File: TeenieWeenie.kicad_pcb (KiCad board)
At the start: 4 copper layers, 50.8 x 101.6 mm, 118 parts, among them J1 Barrel_Jack, J2 Conn_01x01, J3 Conn_01x01, J4 Conn_01x01, J5 Conn_01x01, J6 Conn_01x01, J8 Conn_01x01, Q1 DMP2160UW-7, SW1 SW_Push, U1 WM8904CGEFL/V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

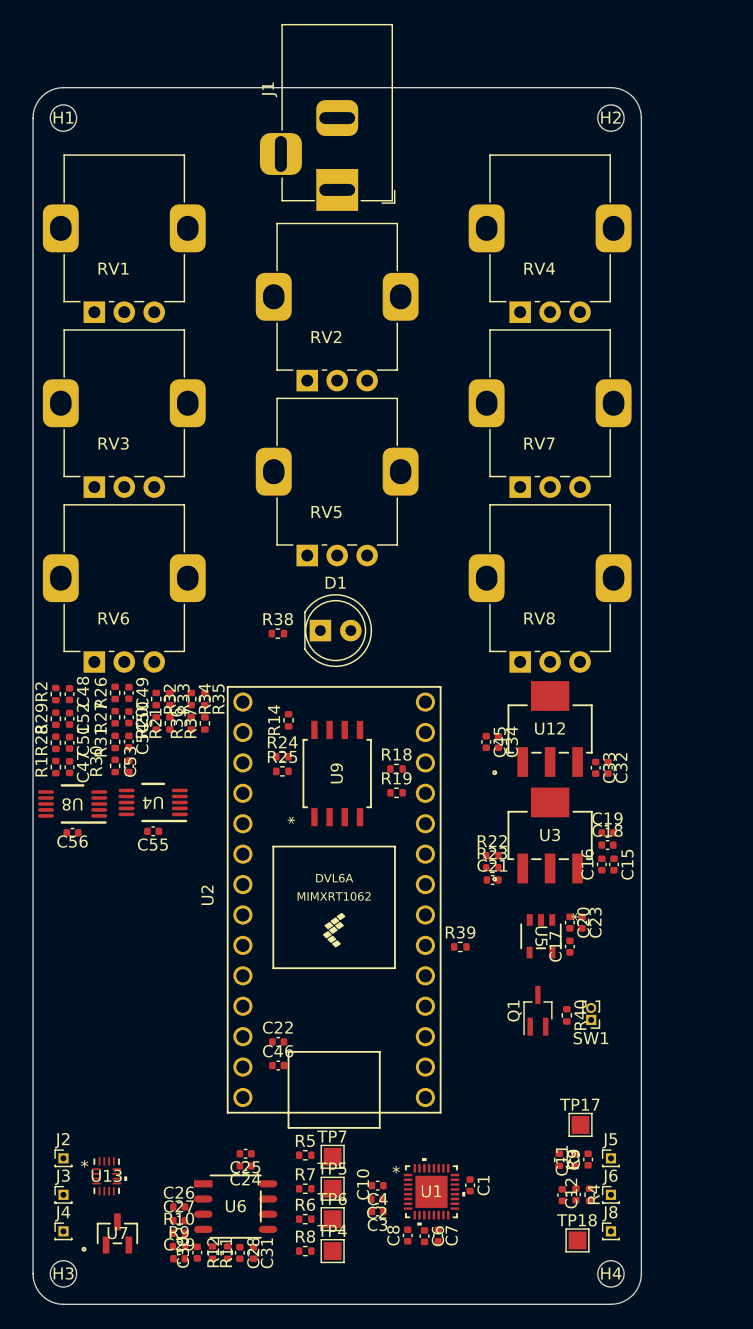
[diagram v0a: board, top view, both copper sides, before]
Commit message: routed power
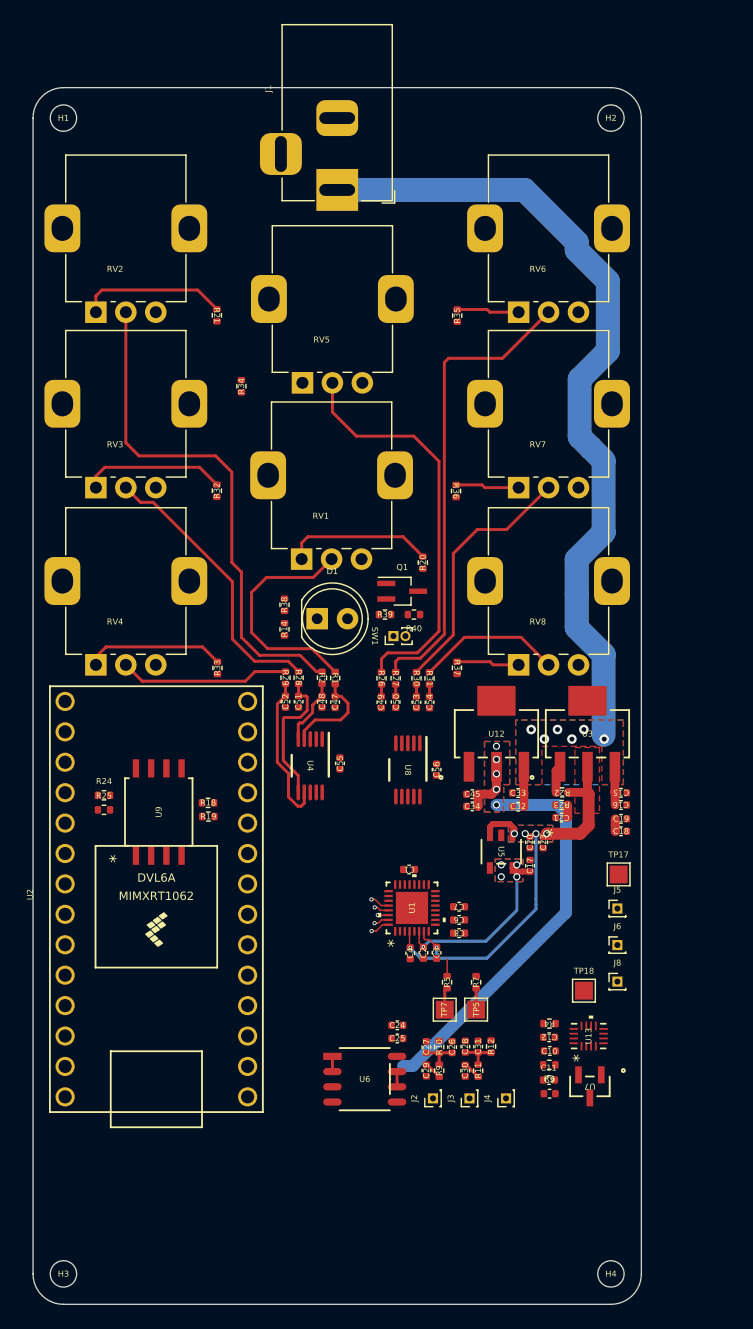
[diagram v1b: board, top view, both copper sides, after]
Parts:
- removed C22: 10u, Capacitor_SMD:C_0402_1005Metric
- removed C46: 0.1u, Capacitor_SMD:C_0402_1005Metric
- removed R6, R8: 0, Resistor_SMD:R_0402_1005Metric
- removed TP4, TP6: TestPoint, TestPoint:TestPoint_Pad_1.5x1.5mm
- moved RV4 46.1 mm to (99.2, 73.6)
- moved RV6 45.9 mm to (134.5, 44.1)
- moved U13 41.9 mm to (140.4, 104.6), turned to 90 degrees
- moved U7 41.3 mm to (140.5, 108.8), turned to 180 degrees
- moved J4 38.6 mm to (133.5, 109.8), turned to 90 degrees
- moved R35 38.3 mm to (129.4, 44.4)
- moved Q1 36.8 mm to (124.8, 67.5), turned to 0 degrees
- moved SW1 36.1 mm to (124.1, 71.2), turned to 90 degrees
- moved R40 35.8 mm to (125.8, 69.4), turned to 180 degrees
- moved J3 34.9 mm to (130.4, 109.8), turned to 90 degrees
- moved R21 34.3 mm to (109.3, 44.4), turned to -90 degrees
- moved J2 31.3 mm to (127.4, 109.8), turned to 90 degrees
- moved C56 30.9 mm to (127.7, 82.3), turned to 90 degrees
- moved R36 29.4 mm to (129.3, 59.1), turned to -90 degrees
- moved R39 28.5 mm to (123.4, 69.4)
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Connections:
- net /AFE/AudioIn_L renamed /AFE/AudioL_Raw
- net /AFE/AudioIn_R renamed /AFE/AudioR_Raw
- net /AudioCodec/AudioOut_L renamed /AudioCodec/AudioL_Dirty
- net /AudioCodec/AudioOut_R renamed /AudioCodec/AudioR_Dirty
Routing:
- net VDD: track 0.00 -> 74.2 mm, vias 0 -> 6
- net /ADC/POT2: track 0.00 -> 42.8 mm
- net /ADC/POT6: track 0.00 -> 39.0 mm
- net +1V8: track 0.00 -> 38.2 mm, vias 0 -> 6
- net +3V3: track 0.00 -> 37.9 mm, vias 0 -> 5
- net /ADC/POT5: track 0.00 -> 34.1 mm
- net /ADC/POT3: track 0.00 -> 23.6 mm
- net /ADC/POT7: track 0.00 -> 21.4 mm
- net /ADC/POT1: track 0.00 -> 19.5 mm
- net +1V0: track 0.00 -> 15.6 mm, vias 0 -> 5
- net /ADC/POT4: track 0.00 -> 14.2 mm
- net /ADC/AIN3_0: track 0.00 -> 12.8 mm
- net Net-(R20-Pad1): track 0.00 -> 12.4 mm
- net Net-(R21-Pad1): track 0.00 -> 12.3 mm
- net /ADC/POT8: track 0.00 -> 12.1 mm
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- added copper zone on B.Cu, net +1V0
- added copper zone on F.Cu, net +1V0
- added copper zone on B.Cu, net +1V8
- added copper zone on F.Cu, net +1V8
- added copper zone on B.Cu, net +3V3
- added copper zone on F.Cu, net +3V3
- added copper zone on In1.Cu, net GND
- added copper zone on In2.Cu, net GND
- added copper zone on B.Cu, net VDD
- added copper zone on F.Cu, net VDD

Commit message: redesign layout
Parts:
- added C13: 1u, Capacitor_SMD:C_0402_1005Metric, F.Cu at (102.0, 107.1)
- added C14: 100n, Capacitor_SMD:C_0402_1005Metric, F.Cu at (102.0, 109.3)
- added C22: 1u, Capacitor_SMD:C_0402_1005Metric, F.Cu at (100.2, 104.2)
- added C5: 1u, Capacitor_SMD:C_0402_1005Metric, F.Cu at (99.9, 112.3)
- added R41: 10k, Resistor_SMD:R_0402_1005Metric, F.Cu at (102.2, 112.3)
- added R42: 10k, Resistor_SMD:R_0402_1005Metric, F.Cu at (101.0, 111.0)
- added R43: 10k, Resistor_SMD:R_0402_1005Metric, F.Cu at (99.9, 108.2)
- added R44: 10k, Resistor_SMD:R_0402_1005Metric, F.Cu at (102.0, 108.2)
- added R45: 10k, Resistor_SMD:R_0402_1005Metric, F.Cu at (101.1, 105.4)
- added R46: 10k, Resistor_SMD:R_0402_1005Metric, F.Cu at (102.5, 104.2)
- added R47: 1M, Resistor_SMD:R_0402_1005Metric, F.Cu at (100.0, 115.3)
- added R48: 1M, Resistor_SMD:R_0402_1005Metric, F.Cu at (100.2, 101.6)
- C10, C9: value 2.2u -> 4.7u
- C26, C28: value 16p -> 10p
- C27, C31: value 160p -> 100p
- R10, R12: value 133k -> 31.1k
- R11, R9: value 7.42k -> 1k
- moved U7 44.8 mm to (96.4, 100.7)
- moved RV5 38.3 mm to (134.3, 84.0)
- moved R34 38.3 mm to (129.1, 84.3)
- moved J4 37.0 mm to (96.5, 110.2), turned to 180 degrees
- moved J3 34.2 mm to (96.5, 114.0), turned to 180 degrees
- moved C30 31.6 mm to (99.9, 116.8), turned to 0 degrees
- moved C28 31.2 mm to (100.0, 113.8), turned to 180 degrees
- moved R12 31.1 mm to (102.2, 113.8), turned to 0 degrees
- moved J2 31.0 mm to (96.5, 106.4), turned to 180 degrees
- moved C31 30.5 mm to (102.3, 115.3), turned to 0 degrees
- moved R11 30.4 mm to (102.2, 116.8), turned to 0 degrees
- moved C26 28.9 mm to (100.2, 102.9), turned to 180 degrees
- moved C29 27.6 mm to (100.2, 100.3), turned to 0 degrees
- moved R9 26.4 mm to (102.5, 100.3), turned to 0 degrees
- moved C53 26.0 mm to (103.4, 89.4)
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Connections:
- C26 pad 1: Net-(C26-Pad1) -> /AFE/IN2+A
- C26 pad 2: GND -> Vdd2
- C27 pad 1: Net-(C26-Pad1) -> Net-(C27-Pad1)
- C27 pad 2: /AFE/AFE_L_0 -> /AFE/OUT2A
- C28 pad 1: Net-(C28-Pad1) -> /AFE/IN1+A
- C28 pad 2: GND -> Vdd2
- C31 pad 1: Net-(C28-Pad1) -> Net-(C31-Pad1)
- C31 pad 2: /AFE/AFE_R_0 -> /AFE/OUT1A
- R10 pad 1: Net-(C26-Pad1) -> Net-(C27-Pad1)
- R10 pad 2: /AFE/NONINV_IN1_0 -> /AFE/IN2+A
- R11 pad 2: Net-(C28-Pad1) -> Net-(C31-Pad1)
- R12 pad 1: Net-(C28-Pad1) -> Net-(C31-Pad1)
- R12 pad 2: /AFE/NONINV_IN2_0 -> /AFE/IN1+A
- R5 pad 2: /AFE/AFE_L_0 -> /AFE/OUT1A
- R7 pad 2: /AFE/AFE_R_0 -> /AFE/OUT2A
- R9 pad 2: Net-(C26-Pad1) -> Net-(C27-Pad1)
- TP5 pad 1: /AFE/AFE_R_0 -> /AFE/OUT2A
- TP7 pad 1: /AFE/AFE_L_0 -> /AFE/OUT1A
- U1 pad 24: Net-(U1-IN2R) -> unconnected-(U1-IN2R-Pad24)
- U1 pad 26: Net-(U1-IN2L) -> unconnected-(U1-IN2L-Pad26)
- U6 pad 1: /AFE/AFE_L_0 -> /AFE/OUT1A
- U6 pad 2: /AFE/AFE_L_0 -> /AFE/IN1+A
- U6 pad 3: /AFE/NONINV_IN1_0 -> /AFE/IN1-A
- U6 pad 5: /AFE/NONINV_IN2_0 -> /AFE/IN2+A
- U6 pad 6: /AFE/AFE_R_0 -> /AFE/IN2-A
- U6 pad 7: /AFE/AFE_R_0 -> /AFE/OUT2A
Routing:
- net /ADC/POT8: track 12.1 -> 56.4 mm
- net /ADC/POT2: track 42.8 -> 0.00 mm
- net +3V3: track 37.9 -> 80.3 mm, vias 5 -> 11
- net /ADC/POT7: track 21.4 -> 53.4 mm
- net /ADC/POT3: track 23.6 -> 0.00 mm
- net /AFE/IN1+A: track 0.00 -> 22.6 mm
- net /AFE/OUT1A: track 0.00 -> 22.4 mm
- net /AFE/AudioR_Raw: track 0.00 -> 19.4 mm
- net /AFE/IN2+A: track 0.00 -> 18.5 mm
- net /AFE/OUT2A: track 0.00 -> 18.3 mm
- net /ADC/POT4: track 14.2 -> 0.00 mm
- net Net-(R20-Pad1): track 12.4 -> 0.00 mm
- net Net-(R21-Pad1): track 12.3 -> 0.00 mm
- net /ADC/SDA: track 0.00 -> 12.0 mm, vias 0 -> 1
- net Net-(R32-Pad1): track 12.0 -> 0.00 mm
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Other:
- board size 50.8 x 101.6 mm -> 50.8 x 88.8 mm

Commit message: routing mostly complete
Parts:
- moved R33 33.3 mm to (109.7, 54.1)
- moved RV2 30.0 mm to (99.5, 84.0)
- moved RV4 30.0 mm to (99.5, 54.0)
- moved TP17 17.6 mm to (138.7, 116.8)
- moved R21 17.4 mm to (109.7, 71.6), turned to 90 degrees
- moved TP18 13.5 mm to (138.9, 104.0)
- moved R25 10.2 mm to (109.3, 98.9)
- moved R24 9.91 mm to (109.3, 100.2)
- moved C12 6.66 mm to (133.8, 105.8), turned to 0 degrees
- moved C10 6.18 mm to (135.9, 105.8), turned to 0 degrees
- moved R4 5.09 mm to (133.8, 106.9), turned to 0 degrees
- moved R43 3.22 mm to (103.1, 107.7), turned to 90 degrees
- moved U13 2.96 mm to (135.9, 109.7), turned to 180 degrees
- moved C14 2.93 mm to (99.6, 107.7), turned to -90 degrees
- moved C9 2.67 mm to (135.8, 113.8), turned to 0 degrees
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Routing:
- net /MCU/~{ADC_IRQ1}: track 0.00 -> 71.3 mm, vias 0 -> 2
- net /AFE/AudioL_Raw: track 9.93 -> 65.6 mm, vias 0 -> 1
- net /AFE/AudioR_Raw: track 19.4 -> 71.6 mm
- net /MCU/~{ADC_IRQ0}: track 0.00 -> 50.7 mm, vias 0 -> 2
- net /MCU/~{SWCTRL}: track 0.00 -> 42.2 mm, vias 0 -> 5
- net /MCU/~{BTN}: track 0.00 -> 39.9 mm
- net /ADC/POT4: track 0.00 -> 38.0 mm
- net /ADC/SDA: track 12.0 -> 47.3 mm, vias 1 -> 2
- net Net-(U2-3_LRCLK2): track 0.00 -> 29.2 mm, vias 0 -> 4
- net /AudioCodec/LINEOUTR: track 0.00 -> 28.6 mm
- net Net-(U2-2_OUT2): track 0.00 -> 28.0 mm
- net +3V3: track 80.3 -> 107.6 mm, vias 11 -> 18
- net Net-(U2-12_MISO_MQSL): track 0.00 -> 24.9 mm
- net /AudioCodec/LINEOUTL: track 0.00 -> 23.1 mm, vias 0 -> 2
- net /ADC/SCL: track 10.7 -> 33.4 mm, vias 1 -> 3
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- added copper zone on B.Cu, net GND
- added copper zone on F.Cu, net GND
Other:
- board size 50.8 x 88.8 mm -> 50.8 x 86.3 mm

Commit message: final manufacturing files
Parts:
- added G***: LOGO, TeenieWeenieLibrary:TeenieWeenieLogo, F.Cu at (108.2, 39.3)
- moved TP17 3.29 mm to (135.4, 116.5)
- moved TP18 2.44 mm to (136.5, 103.6)
- moved C6 0.77 mm to (123.2, 108.4)
- moved C7 0.60 mm to (122.8, 106.5)
- moved C11 0.52 mm to (133.7, 114.3)
- moved C9 0.52 mm to (135.8, 114.3)
- moved R3 0.52 mm to (133.8, 113.1)
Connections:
- C6 pad 2: GND -> +1V0
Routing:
- net +3V3: track 107.6 -> 27.7 mm, vias 18 -> 35
- net Vdd2: track 4.01 -> 19.0 mm
- net GND: track 14.4 -> 23.0 mm, vias 40 -> 75
- net Net-(U1-CPCB): track 0.00 -> 4.89 mm
- net +1V8: track 62.6 -> 66.6 mm
- net VDD: track 74.3 -> 77.7 mm
- net /AFE/AudioR_Raw: track 71.6 -> 74.6 mm
- net /AudioCodec/LINEOUTL: track 23.1 -> 26.0 mm
- net +1V0: track 19.2 -> 21.8 mm, vias 5 -> 6
- net /AudioCodec/LINEOUTR: track 28.6 -> 31.2 mm
- net /AFE/IN2+A: track 18.5 -> 16.6 mm
- net /AFE/IN1+A: track 22.6 -> 21.4 mm
- net /AFE/OUT1A: track 22.4 -> 23.6 mm
- net /AFE/AudioL_Raw: track 65.6 -> 66.2 mm
- net /ADC/SDA: track 47.3 -> 47.8 mm
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- added copper zone on In2.Cu, net +3V3
- removed copper zone on In2.Cu, net GND
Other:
- board text added: "Designed by T. Sweeney"
- board text added: "TeenieWeenie v0.1"
